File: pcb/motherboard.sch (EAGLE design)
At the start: 49 parts

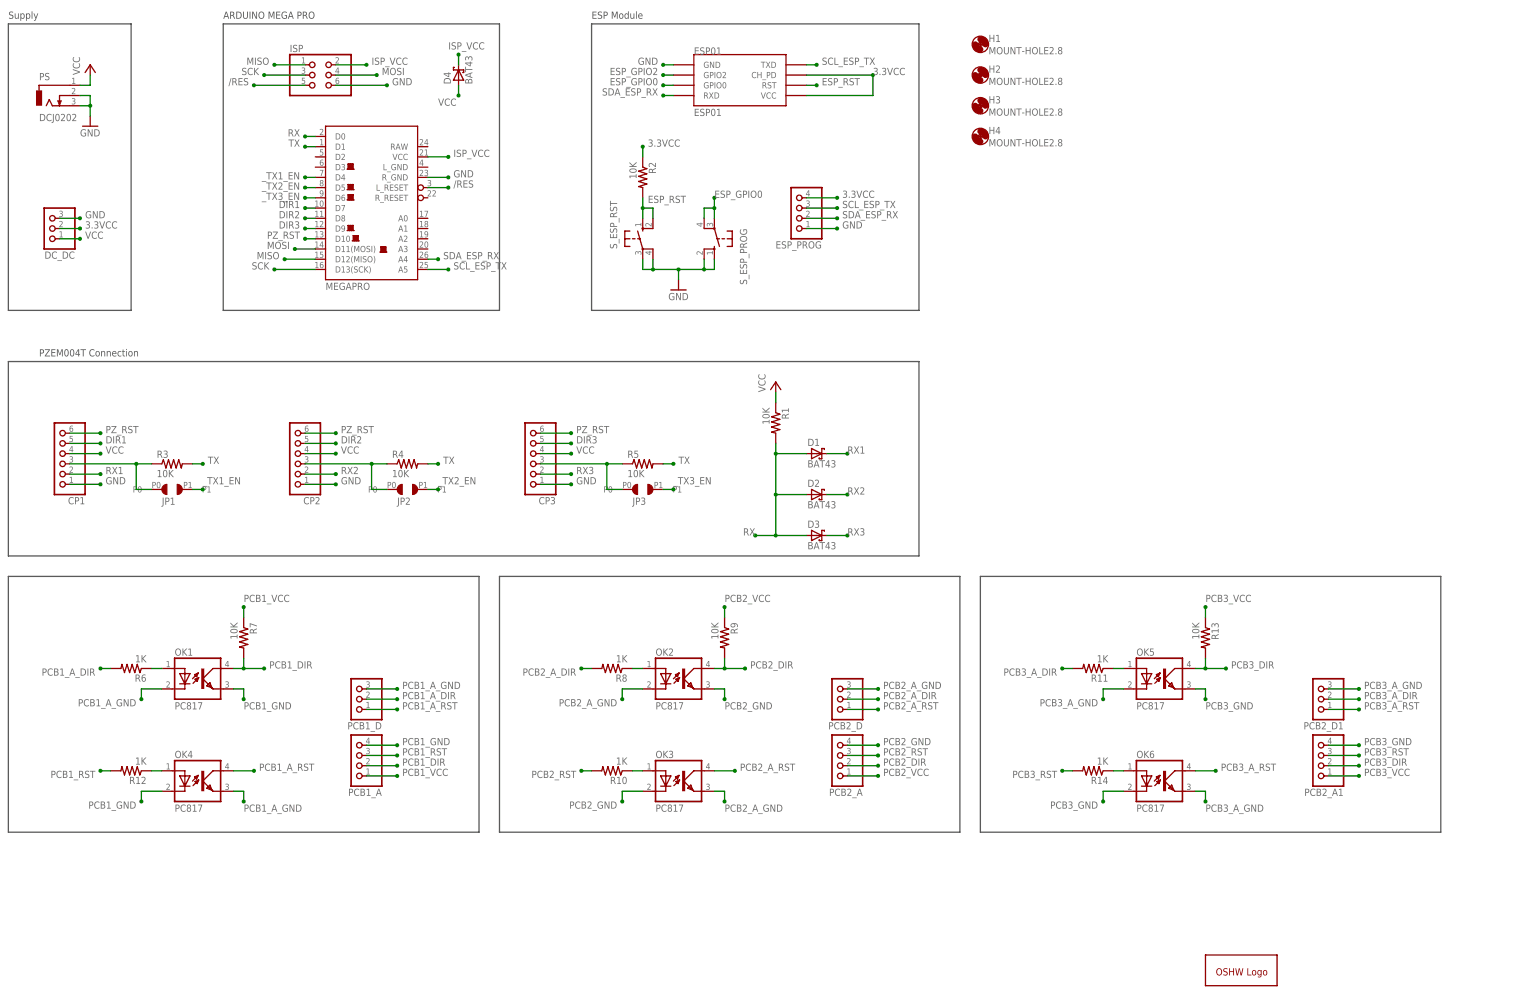
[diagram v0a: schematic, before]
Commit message: Modified to support 6 devices.
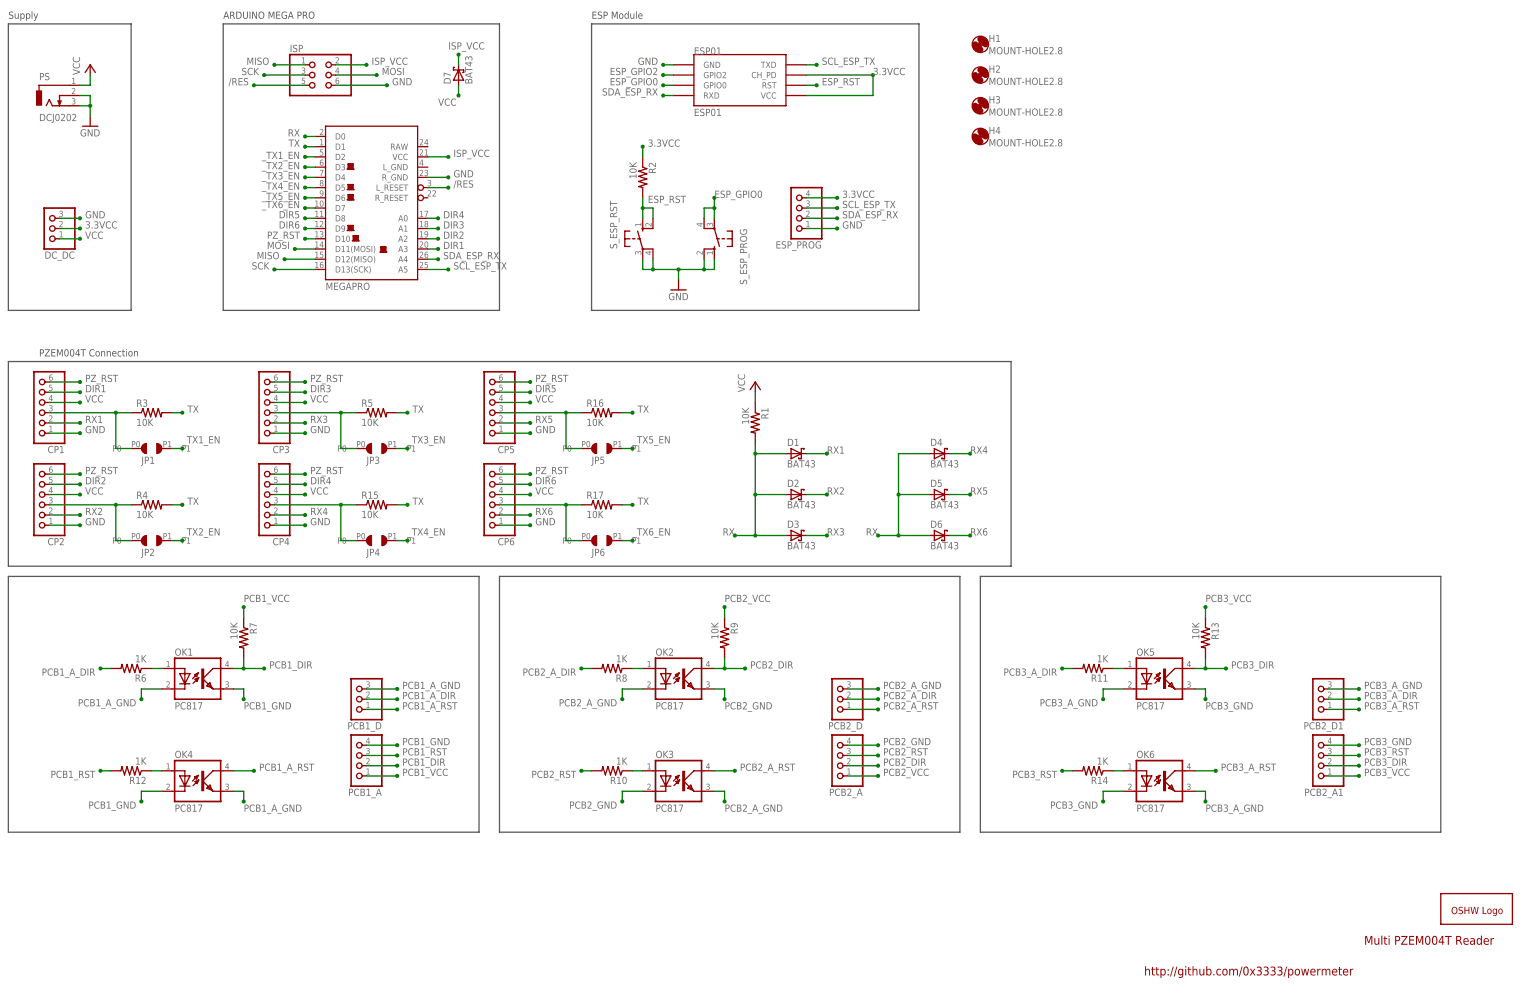
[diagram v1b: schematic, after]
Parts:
- added CP4, CP5, CP6: (no value), pinhead:PINHD-1X6
- added D5, D6, D7: BAT43, diode:BAT60J
- added JP4, JP5, JP6: SMD_JUMPER, EPIC:SMD_JUMPER
- added R15, R16, R17: 10K, resistor:R-US_R1206W
- R1, R3, R4, R5: device resistor:R-US_R0805 -> resistor:R-US_R1206W
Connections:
- new net DIR4: CP4.5, MEGAPRO.A0
- new net DIR5: CP5.5, MEGAPRO.D8
- new net DIR6: CP6.5, MEGAPRO.D9
- new net N$10: CP5.3, JP5.P0, R16.1
- new net N$11: CP6.3, JP6.P0, R17.1
- new net N$9: CP4.3, JP4.P0, R15.1
- new net RX4: CP4.2, D4.C
- new net RX5: CP5.2, D5.C
- new net RX6: CP6.2, D6.C
- new net _TX4_EN: JP4.P1, MEGAPRO.D5
- new net _TX5_EN: JP5.P1, MEGAPRO.D6
- new net _TX6_EN: JP6.P1, MEGAPRO.D7
- net DIR1: now also MEGAPRO.A3; no longer MEGAPRO.D7
- net DIR2: now also MEGAPRO.A2; no longer MEGAPRO.D8
- net DIR3: now also MEGAPRO.A1; no longer MEGAPRO.D9
- net GND: now also CP4.1, CP5.1, CP6.1
- net ISP_VCC: now also D7.C; no longer D4.C
- net PZ_RST: now also CP4.6, CP5.6, CP6.6
- net RX: now also D4.A, D5.A, D6.A
- net TX: now also R15.2, R16.2, R17.2
- net VCC: now also CP4.4, CP5.4, CP6.4, D7.A; no longer D4.A
- net _TX1_EN: now also MEGAPRO.D2; no longer MEGAPRO.D4
- net _TX2_EN: now also MEGAPRO.D3; no longer MEGAPRO.D5
- net _TX3_EN: now also MEGAPRO.D4; no longer MEGAPRO.D6
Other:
- note added: "Multi PZEM004T Reader"
- note added: "http://github.com/0x3333/powermeter"
- moved on the sheet: CP1, CP2, CP3, D1, D2, D3, D4, JP1, JP2, JP3, R1, R3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

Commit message: Updated PCB/Schematic.
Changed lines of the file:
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@@
 <?xml version="1.0" encoding="utf-8"?>
 <!DOCTYPE eagle SYSTEM "eagle.dtd">
-<eagle version="9.1.3">
+<eagle version="9.2.0">
 <drawing>
 <settings>
@@
 <grid distance="0.1" unitdist="inch" unit="inch" style="lines" multiple="1" display="no" altdistance="0.05" altunitdist="inch" altunit="inch"/>
 <layers>
-<layer number="1" name="Top" color="4" fill="1" visible="yes" active="no"/>
-<layer number="16" name="Bottom" color="1" fill="1" visible="yes" active="no"/>
-<layer number="17" name="Pads" color="2" fill="1" visible="yes" active="no"/>
-<layer number="18" name="Vias" color="2" fill="1" visible="yes" active="no"/>
-<layer number="19" name="Unrouted" color="6" fill="1" visible="yes" active="no"/>
-<layer number="20" name="Dimension" color="24" fill="1" visible="yes" active="no"/>
-<layer number="21" name="tPlace" color="7" fill="1" visible="yes" active="no"/>
-<layer number="22" name="bPlace" color="7" fill="1" visible="yes" active="no"/>
-<layer number="23" name="tOrigins" color="15" fill="1" visible="yes" active="no"/>
-<layer number="24" name="bOrigins" color="15" fill="1" visible="yes" active="no"/>
-<layer number="25" name="tNames" color="7" fill="1" visible="yes" active="no"/>
-<layer number="26" name="bNames" color="7" fill="1" visible="yes" active="no"/>
-<layer number="27" name="tValues" color="7" fill="1" visible="yes" active="no"/>
-<layer number="28" name="bValues" color="7" fill="1" visible="yes" active="no"/>
+<layer number="1" name="Top" color="4" fill="1" visible="no" active="no"/>
+<layer number="16" name="Bottom" color="1" fill="1" visible="no" active="no"/>
+<layer number="17" name="Pads" color="2" fill="1" visible="no" active="no"/>
+<layer number="18" name="Vias" color="2" fill="1" visible="no" active="no"/>
+<layer number="19" name="Unrouted" color="6" fill="1" visible="no" active="no"/>
+<layer number="20" name="Dimension" color="24" fill="1" visible="no" active="no"/>
+<layer number="21" name="tPlace" color="7" fill="1" visible="no" active="no"/>
+<layer number="22" name="bPlace" color="7" fill="1" visible="no" active="no"/>
+<layer number="23" name="tOrigins" color="15" fill="1" visible="no" active="no"/>
+<layer number="24" name="bOrigins" color="15" fill="1" visible="no" active="no"/>
+<layer number="25" name="tNames" color="7" fill="1" visible="no" active="no"/>
+<layer number="26" name="bNames" color="7" fill="1" visible="no" active="no"/>
+<layer number="27" name="tValues" color="7" fill="1" visible="no" active="no"/>
+<layer number="28" name="bValues" color="7" fill="1" visible="no" active="no"/>
 <layer number="29" name="tStop" color="7" fill="3" visible="no" active="no"/>
 <layer number="30" name="bStop" color="7" fill="6" visible="no" active="no"/>
@@
 <layer number="35" name="tGlue" color="7" fill="4" visible="no" active="no"/>
 <layer number="36" name="bGlue" color="7" fill="5" visible="no" active="no"/>
-<layer number="37" name="tTest" color="7" fill="1" visible="yes" active="no"/>
-<layer number="38" name="bTest" color="7" fill="1" visible="yes" active="no"/>
+<layer number="37" name="tTest" color="7" fill="1" visible="no" active="no"/>
+<layer number="38" name="bTest" color="7" fill="1" visible="no" active="no"/>
 <layer number="39" name="tKeepout" color="4" fill="11" visible="no" active="no"/>
 <layer number="40" name="bKeepout" color="1" fill="11" visible="no" active="no"/>
@@
 <layer number="44" name="Drills" color="7" fill="1" visible="no" active="no"/>
 <layer number="45" name="Holes" color="7" fill="1" visible="no" active="no"/>
-<layer number="46" name="Milling" color="3" fill="1" visible="yes" active="no"/>
-<layer number="47" name="Measures" color="7" fill="1" visible="yes" active="no"/>
-<layer number="48" name="Document" color="7" fill="1" visible="yes" active="no"/>
-<layer number="49" name="Reference" color="7" fill="1" visible="yes" active="no"/>
-<layer number="50" name="dxf" color="7" fill="1" visible="yes" active="no"/>
-<layer number="51" name="tDocu" color="7" fill="1" visible="yes" active="no"/>
-<layer number="52" name="bDocu" color="7" fill="1" visible="yes" active="no"/>
-<layer number="53" name="tGND_GNDA" color="7" fill="9" visible="yes" active="no"/>
-<layer number="54" name="bGND_GNDA" color="1" fill="9" visible="yes" active="no"/>
-<layer number="56" name="wert" color="3" fill="1" visible="yes" active="no"/>
-<layer number="57" name="tCAD" color="7" fill="1" visible="yes" active="no"/>
-<layer number="59" name="tCarbon" color="7" fill="1" visible="yes" active="no"/>
-<layer number="60" name="bCarbon" color="7" fill="1" visible="yes" active="no"/>
+<layer number="46" name="Milling" color="3" fill="1" visible="no" active="no"/>
+<layer number="47" name="Measures" color="7" fill="1" visible="no" active="no"/>
+<layer number="48" name="Document" color="7" fill="1" visible="no" active="no"/>
+<layer number="49" name="Reference" color="7" fill="1" visible="no" active="no"/>
+<layer number="50" name="dxf" color="7" fill="1" visible="no" active="no"/>
+<layer number="51" name="tDocu" color="7" fill="1" visible="no" active="no"/>
+<layer number="52" name="bDocu" color="7" fill="1" visible="no" active="no"/>
+<layer number="53" name="tGND_GNDA" color="7" fill="9" visible="no" active="no"/>
+<layer number="54" name="bGND_GNDA" color="1" fill="9" visible="no" active="no"/>
+<layer number="56" name="wert" color="3" fill="1" visible="no" active="no"/>
+<layer number="57" name="tCAD" color="7" fill="1" visible="no" active="no"/>
+<layer number="59" name="tCarbon" color="7" fill="1" visible="no" active="no"/>
+<layer number="60" name="bCarbon" color="7" fill="1" visible="no" active="no"/>
 <layer number="88" name="SimResults" color="9" fill="1" visible="yes" active="yes"/>
 <layer number="89" name="SimProbes" color="9" fill="1" visible="yes" active="yes"/>
@@
 <instances>
 <instance part="FRAME1" gate="G$1" x="0" y="0">
-<attribute name="SHEET" x="375.285" y="5.08" size="2.54" layer="94"/>
+<attribute name="DRAWING_NAME" x="344.17" y="15.24" size="2.54" layer="94"/>
+<attribute name="LAST_DATE_TIME" x="344.17" y="10.16" size="2.286" layer="94"/>
+<attribute name="SHEET" x="357.505" y="5.08" size="2.54" layer="94"/>
 </instance>
 <instance part="MEGAPRO" gate="G$1" x="99.06" y="208.28">
@@
 <instance part="GOLD_ORB_SM1" gate="G$1" x="363.22" y="25.4"/>
 <instance part="JP1" gate="G$1" x="43.18" y="143.51">
-<attribute name="NAME" x="40.64" y="139.7" size="1.778" layer="96"/>
+<attribute name="NAME" x="40.64" y="146.05" size="1.778" layer="96"/>
 </instance>
 <instance part="JP2" gate="G$1" x="43.18" y="120.65">
-<attribute name="NAME" x="40.64" y="116.84" size="1.778" layer="96"/>
+<attribute name="NAME" x="40.64" y="123.19" size="1.778" layer="96"/>
 </instance>
 <instance part="JP3" gate="G$1" x="99.06" y="143.51">
-<attribute name="NAME" x="96.52" y="139.7" size="1.778" layer="96"/>
+<attribute name="NAME" x="96.52" y="146.05" size="1.778" layer="96"/>
 </instance>
 <instance part="OK1" gate="A" x="55.88" y="86.36">
@@
 </instance>
 <instance part="JP4" gate="G$1" x="99.06" y="120.65">
-<attribute name="NAME" x="96.52" y="116.84" size="1.778" layer="96"/>
+<attribute name="NAME" x="96.52" y="123.19" size="1.778" layer="96"/>
 </instance>
 <instance part="CP5" gate="A" x="127" y="154.94" rot="R180">
@@
 </instance>
 <instance part="JP5" gate="G$1" x="154.94" y="143.51">
-<attribute name="NAME" x="152.4" y="139.7" size="1.778" layer="96"/>
+<attribute name="NAME" x="152.4" y="146.05" size="1.778" layer="96"/>
 </instance>
 <instance part="CP6" gate="A" x="127" y="132.08" rot="R180">
@@
 </instance>
 <instance part="JP6" gate="G$1" x="154.94" y="120.65">
-<attribute name="NAME" x="152.4" y="116.84" size="1.778" layer="96"/>
+<attribute name="NAME" x="152.4" y="123.19" size="1.778" layer="96"/>
 </instance>
 </instances>
